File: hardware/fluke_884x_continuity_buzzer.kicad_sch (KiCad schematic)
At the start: 70 parts, among them J2 Conn_01x02, J203 16 pin DIP socket, J204 16 pin DIP socket, J3 USB_B_Micro, P203 16 pin DIP plug, P204 16 pin DIP plug, U1 AZ117EH-3.3, U2 W25Q128JVS, U3 RP2040, Y1 ABLS-12.000MHZ-B4-T

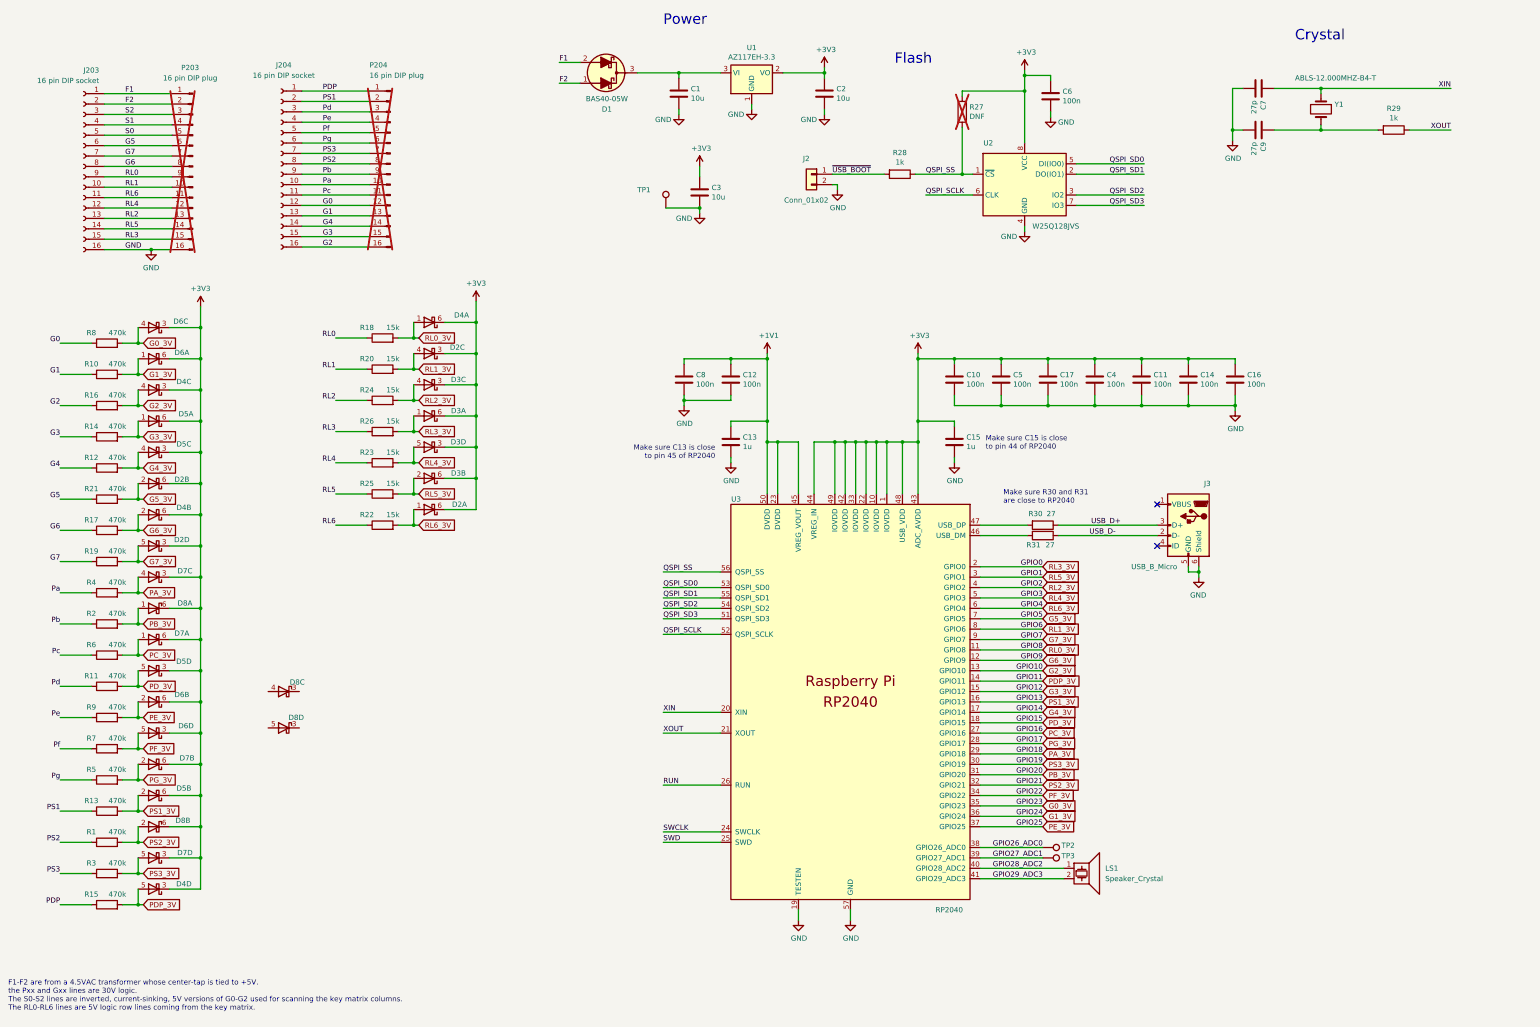
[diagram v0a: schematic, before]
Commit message: WIP: made board shorter
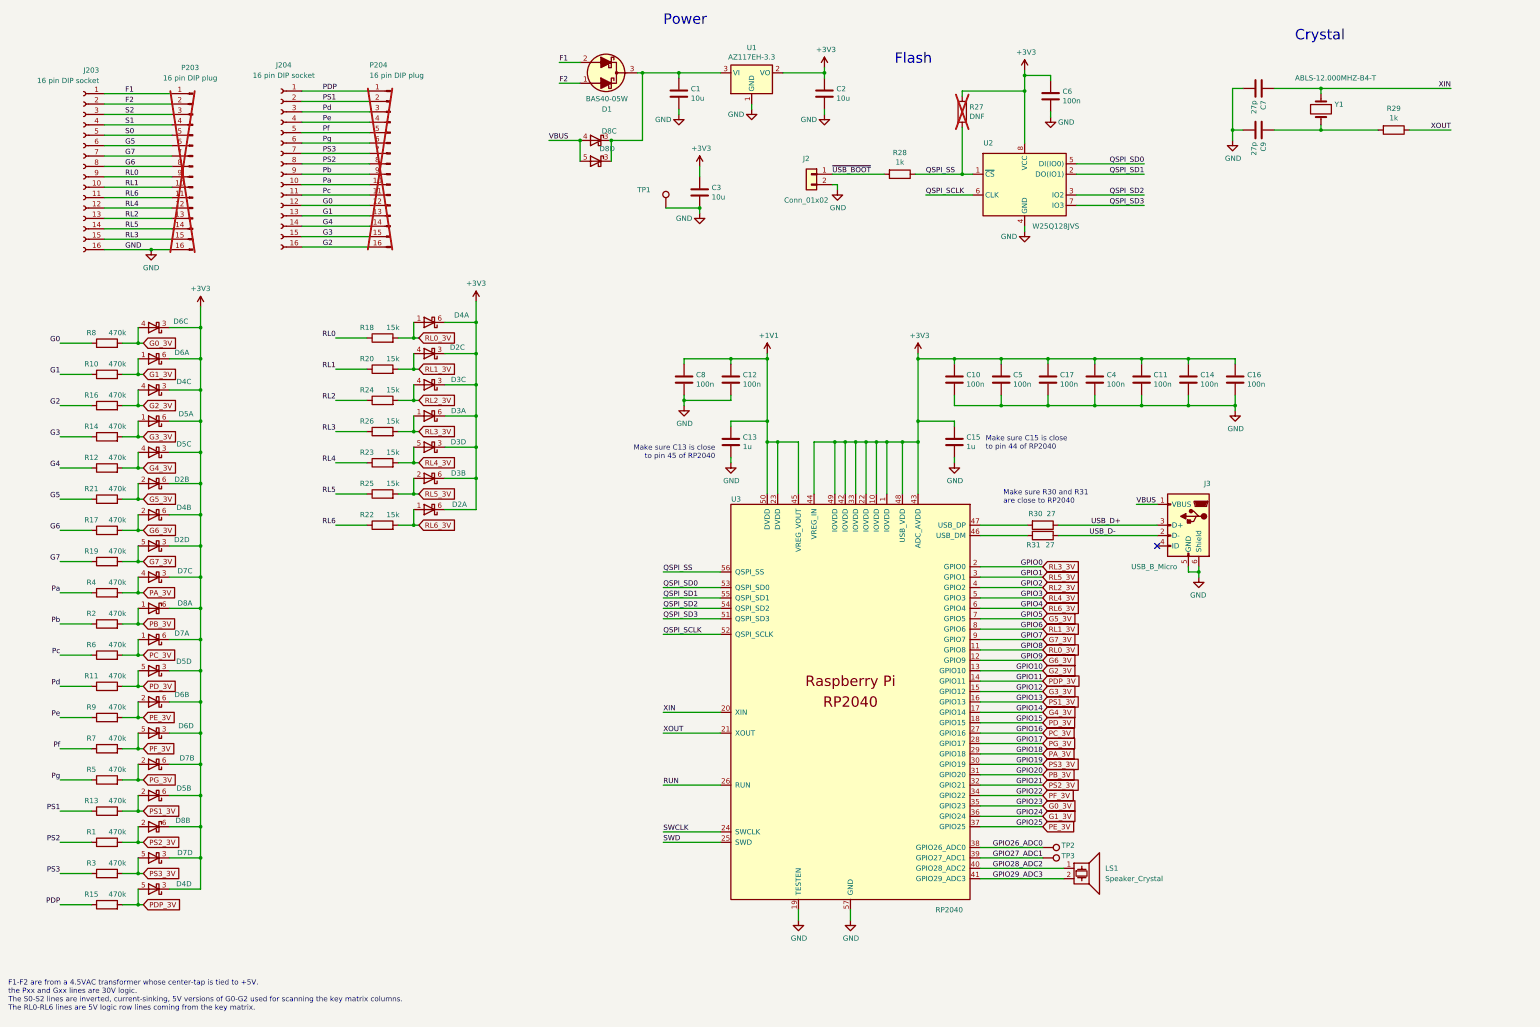
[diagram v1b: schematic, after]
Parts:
- R27: now left out of the parts list
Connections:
- net at D8.3 (K): now also C1.1, D1.3 (K), D8.3 (K), U1.3 (VI)
- net VBUS: now reaches D8.4 (A)
- net VBUS: now also D8.5 (A), J3.1 (VBUS)
- no-connect marks 2 -> 1
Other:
- moved on the sheet: D8C, D8D
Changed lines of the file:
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@@
 	)
 	(junction
+		(at 163.83 48.26)
+		(diameter 0)
+		(color 0 0 0 0)
+	)
+	(junction
 		(at 48.26 189.23)
 		(diameter 0)
@@
 	)
 	(junction
+		(at 156.21 48.26)
+		(diameter 0)
+		(color 0 0 0 0)
+	)
+	(junction
 		(at 48.26 204.47)
 		(diameter 0)
@@
 	)
 	(junction
+		(at 171.45 31.75)
+		(diameter 0)
+		(color 0 0 0 0)
+	)
+	(junction
 		(at 48.26 158.75)
 		(diameter 0)
@@
 		(at 297.18 147.32)
 	)
-	(no_connect
-		(at 297.18 137.16)
-	)
 	(wire
 		(pts
@@
 	(wire
 		(pts
+			(xy 171.45 48.26) (xy 171.45 31.75)
+		)
+		(stroke
+			(width 0)
+			(type default)
+		)
+	)
+	(wire
+		(pts
 			(xy 247.65 102.87) (xy 247.65 101.6)
 		)
@@
 	(wire
 		(pts
+			(xy 292.1 137.16) (xy 297.18 137.16)
+		)
+		(stroke
+			(width 0)
+			(type default)
+		)
+	)
+	(wire
+		(pts
 			(xy 304.8 113.03) (xy 293.37 113.03)
 		)
@@
 	(wire
 		(pts
+			(xy 163.83 48.26) (xy 163.83 53.34)
+		)
+		(stroke
+			(width 0)
+			(type default)
+		)
+	)
+	(wire
+		(pts
 			(xy 264.795 32.385) (xy 264.795 36.195)
 		)
@@
 	(wire
 		(pts
+			(xy 171.45 31.75) (xy 180.34 31.75)
+		)
+		(stroke
+			(width 0)
+			(type default)
+		)
+	)
+	(wire
+		(pts
 			(xy 44.45 166.37) (xy 48.26 166.37)
 		)
@@
 	(wire
 		(pts
+			(xy 156.21 48.26) (xy 156.21 53.34)
+		)
+		(stroke
+			(width 0)
+			(type default)
+		)
+	)
+	(wire
+		(pts
 			(xy 238.76 101.6) (xy 238.76 116.84)
 		)
@@
 	(wire
 		(pts
+			(xy 163.83 48.26) (xy 171.45 48.26)
+		)
+		(stroke
+			(width 0)
+			(type default)
+		)
+	)
+	(wire
+		(pts
 			(xy 316.23 102.87) (xy 316.23 101.6)
 		)
@@
 	(wire
 		(pts
-			(xy 170.18 31.75) (xy 180.34 31.75)
+			(xy 170.18 31.75) (xy 171.45 31.75)
 		)
 		(stroke
@@
 	(wire
 		(pts
+			(xy 148.59 48.26) (xy 156.21 48.26)
+		)
+		(stroke
+			(width 0)
+			(type default)
+		)
+	)
+	(wire
+		(pts
 			(xy 63.5 101.6) (xy 55.88 101.6)
 		)
@@
 		)
 	)
+	(label "VBUS"
+		(at 148.59 48.26 0)
+		(fields_autoplaced yes)
+		(effects
+			(font
+				(size 1.27 1.27)
+			)
+			(justify left bottom)
+		)
+	)
 	(label "GPIO24"
 		(at 269.24 213.36 180)
@@
 		)
 	)
+	(label "VBUS"
+		(at 292.1 137.16 0)
+		(fields_autoplaced yes)
+		(effects
+			(font
+				(size 1.27 1.27)
+			)
+			(justify left bottom)
+		)
+	)
 	(label "Pe"
 		(at 93.345 43.815 0)
@@
 	(symbol
 		(lib_id "misc:BAT54CDW")
-		(at 83.82 182.88 180)
+		(at 160.02 48.26 180)
 		(unit 3)
 		(exclude_from_sim no)
@@
 		(dnp no)
 		(property "Reference" "D8"
-			(at 87.122 180.594 0)
+			(at 163.322 45.974 0)
 			(effects
 				(font
@@
 		)
 		(property "Value" "BAT54CDW"
-			(at 84.1375 179.07 0)
+			(at 160.3375 44.45 0)
 			(effects
 				(font
@@
 		)
 		(property "Footprint" "Package_TO_SOT_SMD:SOT-363_SC-70-6"
-			(at 83.82 178.435 0)
+			(at 160.02 43.815 0)
 			(effects
 				(font
@@
 		)
 		(property "Datasheet" "https://www.diodes.com/assets/Datasheets/BAT54TW_ADW_CDW_SDW_BRW.pdf"
-			(at 83.82 185.42 0)
+			(at 160.02 50.8 0)
 			(effects
 				(font
@@
 		)
 		(property "Description" "Schottky diode array 2 pair Com C, SOT-363"
-			(at 83.82 182.88 0)
+			(at 160.02 48.26 0)
 			(effects
 				(font
@@
 		)
 		(property "LCSC" "C5240639"
-			(at 83.82 182.88 0)
+			(at 160.02 48.26 0)
 			(effects
 				(font
@@
 		)
 		(property "Field-1" ""
-			(at 83.82 182.88 0)
+			(at 160.02 48.26 0)
 			(effects
 				(font
@@
 		(unit 1)
 		(exclude_from_sim no)
-		(in_bom yes)
+		(in_bom no)
 		(on_board yes)
 		(dnp yes)
@@
 	(symbol
 		(lib_id "misc:BAT54CDW")
-		(at 83.82 191.77 180)
+		(at 160.02 53.34 180)
 		(unit 4)
 		(exclude_from_sim no)
@@
 		(dnp no)
 		(property "Reference" "D8"
-			(at 86.868 189.23 0)
+			(at 162.814 50.292 0)
 			(effects
 				(font
@@
 		)
 		(property "Value" "BAT54CDW"
-			(at 84.1375 187.96 0)
+			(at 160.3375 49.53 0)
 			(effects
 				(font
@@
 		)
 		(property "Footprint" "Package_TO_SOT_SMD:SOT-363_SC-70-6"
-			(at 83.82 187.325 0)
+			(at 160.02 48.895 0)
 			(effects
 				(font
@@
 		)
 		(property "Datasheet" "https://www.diodes.com/assets/Datasheets/BAT54TW_ADW_CDW_SDW_BRW.pdf"
-			(at 83.82 194.31 0)
+			(at 160.02 55.88 0)
 			(effects
 				(font
@@
 		)
 		(property "Description" "Schottky diode array 2 pair Com C, SOT-363"
-			(at 83.82 191.77 0)
+			(at 160.02 53.34 0)
 			(effects
 				(font
@@
 		)
 		(property "LCSC" "C5240639"
-			(at 83.82 191.77 0)
+			(at 160.02 53.34 0)
 			(effects
 				(font
@@
 		)
 		(property "Field-1" ""
-			(at 83.82 191.77 0)
+			(at 160.02 53.34 0)
 			(effects
 				(font

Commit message: WIP: shortened board, added driver for keypad signals.
Also changed 30V R values.
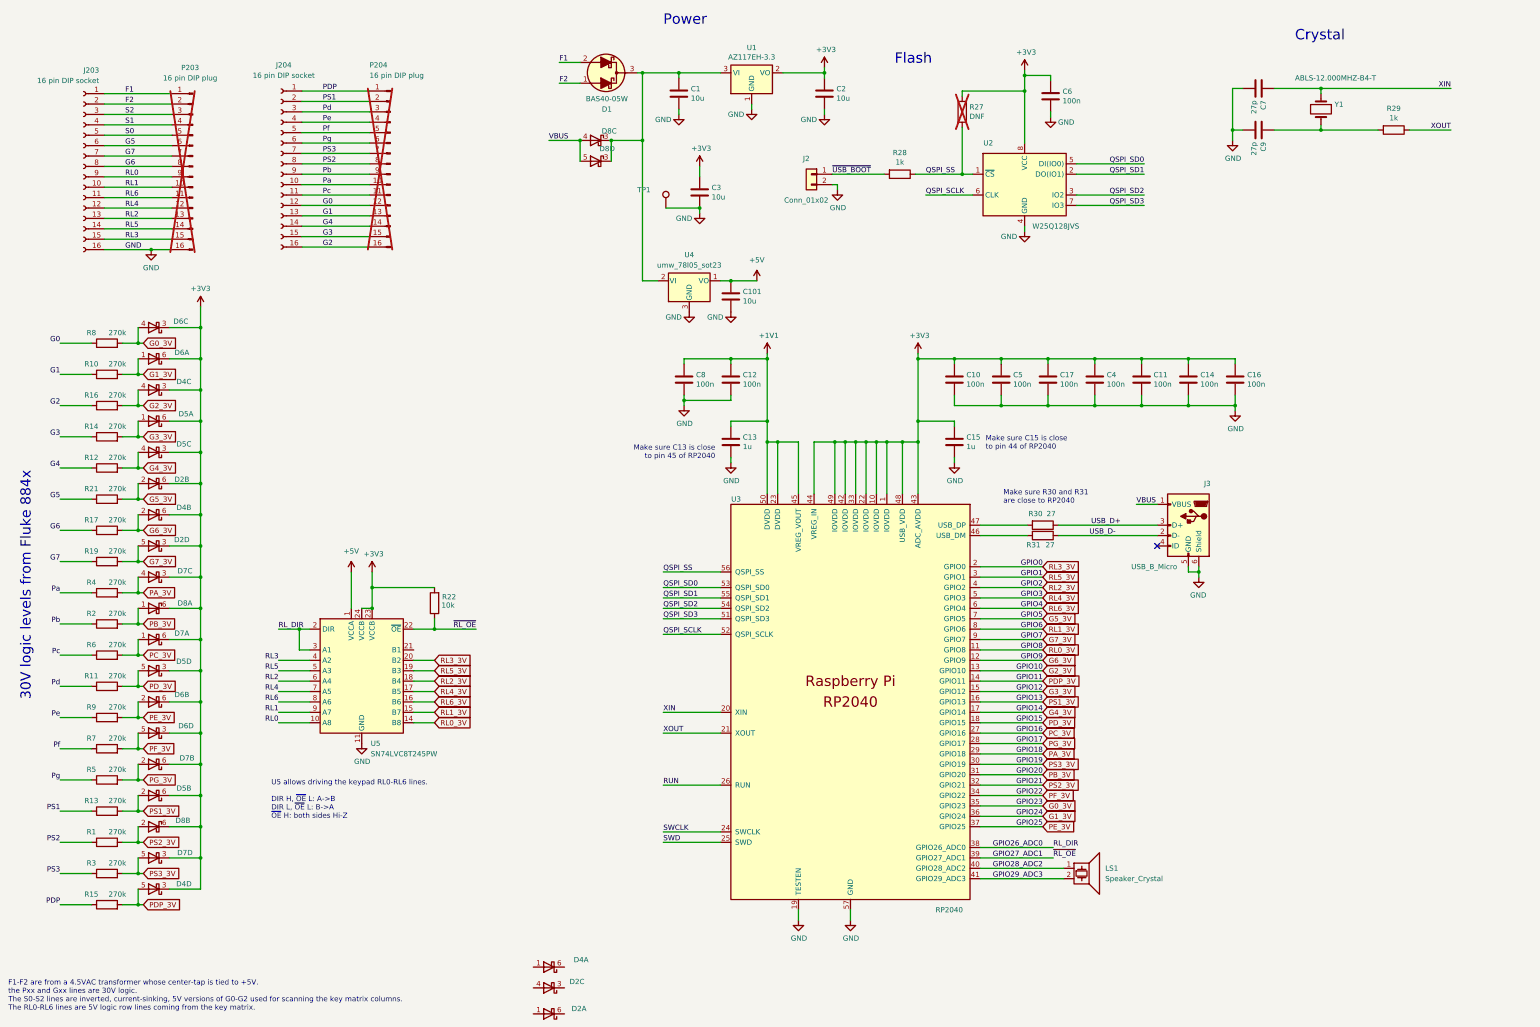
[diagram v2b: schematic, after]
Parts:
- removed D3: BAT54CDW, Package_TO_SOT_SMD:SOT-363_SC-70-6, symbol misc:BAT54CDW
- removed R18, R20, R23, R24, R25, R26: 15k, Resistor_SMD:R_0402_1005Metric, symbol Device:R
- removed TP2, TP3: TestPoint, TestPoint:TestPoint_THTPad_D1.0mm_Drill0.5mm, symbol Connector:TestPoint
- added C101: 10u, Capacitor_SMD:C_0805_2012Metric, symbol Device:C
- added U4: umw_78l05_sot23, Package_TO_SOT_SMD:SOT-23-3, symbol misc:umw_78l05_sot23
- added U5: SN74LVC8T245PW, Package_SO:TSSOP-24_4.4x7.8mm_P0.65mm, symbol Logic_LevelTranslator:SN74AVC8T245PW
- R1, R10, R11, R12, R13, R14, R15, R16, R17, R19, R2, R21, R3, R4, R5, R6, R7, R8, R9: value 470k -> 270k
- R22: value 15k -> 10k; LCSC C25756 -> (none)
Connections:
- net +3V3: now also R22.2, U5.23 (VCCB), U5.24 (VCCB); no longer D2.3 (K), D2.6 (K), D4.6 (K)
- net GND: now also C101.2, U4.3 (GND), U5.11 (GND), U5.12 (GND), U5.13 (GND)
- net GPIO26_ADC0: now also U5.2 (DIR), U5.3 (A1)
- net GPIO27_ADC1: now also R22.1, U5.22 (~{OE})
- net RL0: now also U5.10 (A8)
- net RL0_3V: now also U5.14 (B8); no longer D4.1 (A)
- net RL1: now also U5.9 (A7)
- net RL1_3V: now also U5.15 (B7); no longer D2.4 (A)
- net RL2: now also U5.6 (A4)
- net RL2_3V: now also U5.18 (B4)
- net RL3: now also U5.4 (A2)
- net RL3_3V: now also U5.20 (B2)
- net RL4: now also U5.7 (A5)
- net RL4_3V: now also U5.17 (B5)
- net RL5: now also U5.5 (A3)
- net RL5_3V: now also U5.19 (B3)
- net RL6: now also U5.8 (A6); no longer R22.1
- net RL6_3V: now also U5.16 (B6); no longer D2.1 (A), R22.2
- net at C1.1, D1.3 (K), D8.3 (K)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: now also U4.2 (VI)
- new net +5V: C101.1, U4.1 (VO), U5.1 (VCCA)
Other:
- note added: "30V logic levels from Fluke 884x"
- note added: "U5 allows driving the keypad RL0-RL6 lines. DIR H, ~{OE} L: A->B DIR L, ~{OE} L: B->A ~{OE} H: both sides Hi-Z"
- moved on the sheet: D2A, D2C, D4A

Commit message: Update JLC part numbers
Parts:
- R1, R10, R11, R12, R13, R14, R15, R16, R17, R19, R2, R21, R3, R4, R5, R6, R7, R8, R9: LCSC C25790 -> C25550
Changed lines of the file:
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@@
 			)
 		)
-		(property "LCSC" "C25790"
+		(property "LCSC" "C25550"
 			(at 40.64 105.41 0)
 			(effects
@@
 			)
 		)
-		(property "LCSC" "C25790"
+		(property "LCSC" "C25550"
 			(at 40.64 234.95 0)
 			(effects
@@
 			)
 		)
-		(property "LCSC" "C25790"
+		(property "LCSC" "C25550"
 			(at 40.64 181.61 0)
 			(effects
@@
 			)
 		)
-		(property "LCSC" "C25790"
+		(property "LCSC" "C25550"
 			(at 40.64 166.37 0)
 			(effects
@@
 			)
 		)
-		(property "LCSC" "C25790"
+		(property "LCSC" "C25550"
 			(at 40.64 189.23 0)
 			(effects
@@
 			)
 		)
-		(property "LCSC" "C25790"
+		(property "LCSC" "C25550"
 			(at 40.64 158.75 0)
 			(effects
@@
 			)
 		)
-		(property "LCSC" "C25790"
+		(property "LCSC" "C25550"
 			(at 40.64 212.09 0)
 			(effects
@@
 			)
 		)
-		(property "LCSC" "C25790"
+		(property "LCSC" "C25550"
 			(at 40.64 128.27 0)
 			(effects
@@
 			)
 		)
-		(property "LCSC" "C25790"
+		(property "LCSC" "C25550"
 			(at 40.64 97.79 0)
 			(effects
@@
 			)
 		)
-		(property "LCSC" "C25790"
+		(property "LCSC" "C25550"
 			(at 40.64 227.33 0)
 			(effects
@@
 			)
 		)
-		(property "LCSC" "C25790"
+		(property "LCSC" "C25550"
 			(at 40.64 173.99 0)
 			(effects
@@
 			)
 		)
-		(property "LCSC" "C25790"
+		(property "LCSC" "C25550"
 			(at 40.64 113.03 0)
 			(effects
@@
 			)
 		)
-		(property "LCSC" "C25790"
+		(property "LCSC" "C25550"
 			(at 40.64 204.47 0)
 			(effects
@@
 			)
 		)
-		(property "LCSC" "C25790"
+		(property "LCSC" "C25550"
 			(at 40.64 151.13 0)
 			(effects
@@
 			)
 		)
-		(property "LCSC" "C25790"
+		(property "LCSC" "C25550"
 			(at 40.64 120.65 0)
 			(effects
@@
 			)
 		)
-		(property "LCSC" "C25790"
+		(property "LCSC" "C25550"
 			(at 40.64 196.85 0)
 			(effects
@@
 			)
 		)
-		(property "LCSC" "C25790"
+		(property "LCSC" "C25550"
 			(at 40.64 219.71 0)
 			(effects
@@
 			)
 		)
-		(property "LCSC" "C25790"
+		(property "LCSC" "C25550"
 			(at 40.64 135.89 0)
 			(effects
@@
 			)
 		)
-		(property "LCSC" "C25790"
+		(property "LCSC" "C25550"
 			(at 40.64 143.51 0)
 			(effects
